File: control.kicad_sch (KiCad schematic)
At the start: 6 parts

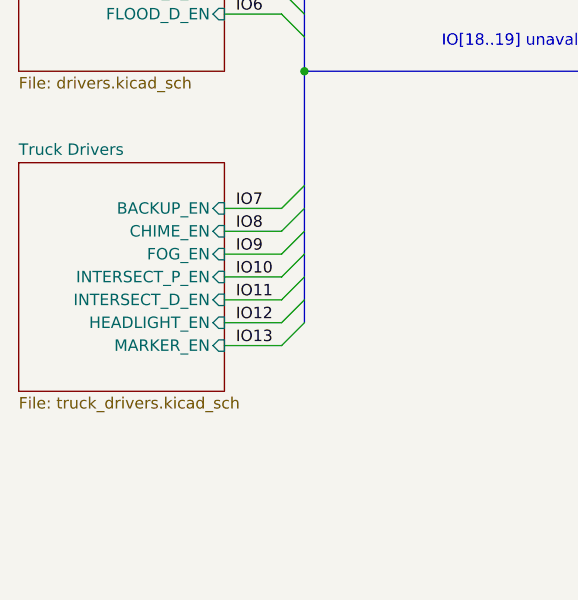
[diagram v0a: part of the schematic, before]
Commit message: add horn circuit
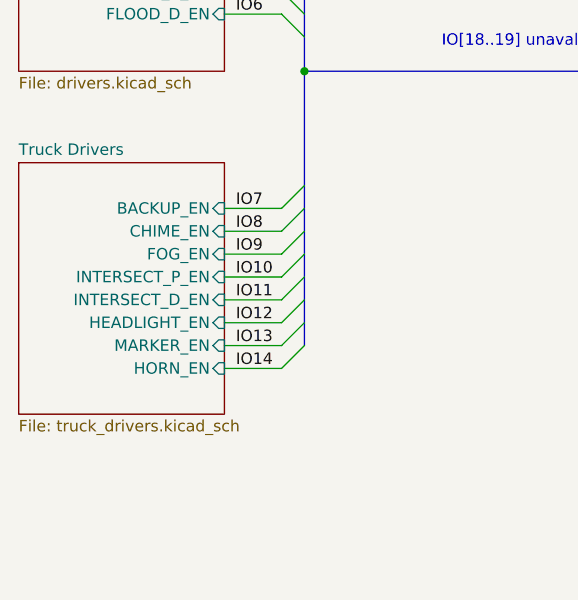
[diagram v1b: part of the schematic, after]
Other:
- sheet Truck Drivers ports: added HORN_EN; removed none
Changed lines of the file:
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@@
+    (stroke (width 0) (type default) (color 0 0 0 0))
+  )
+  (bus_entry (at 86.36 120.65) (size 2.54 -2.54)
     (stroke (width 0) (type default) (color 0 0 0 0))
   )
@@
     (stroke (width 0) (type default) (color 0 0 0 0))
   )
+  (bus (pts (xy 88.9 115.57) (xy 88.9 118.11))
+    (stroke (width 0) (type default) (color 0 0 0 0))
+  )
   (wire (pts (xy 234.95 147.32) (xy 237.49 147.32))
     (stroke (width 0) (type default) (color 0 0 0 0))
@@
   )
   (wire (pts (xy 234.95 144.78) (xy 237.49 144.78))
+    (stroke (width 0) (type default) (color 0 0 0 0))
+  )
+  (wire (pts (xy 80.01 120.65) (xy 86.36 120.65))
     (stroke (width 0) (type default) (color 0 0 0 0))
   )
@@
   )
   (label "IO4" (at 186.69 46.99 0)
+    (effects (font (size 1.27 1.27)) (justify left bottom))
+  )
+  (label "IO14" (at 81.28 120.65 0)
     (effects (font (size 1.27 1.27)) (justify left bottom))
   )
@@
     )
   )
-  (sheet (at 57.15 97.79) (size 22.86 25.4) (fields_autoplaced)
+  (sheet (at 57.15 97.79) (size 22.86 27.94) (fields_autoplaced)
     (stroke (width 0.1524) (type solid) (color 0 0 0 0))
     (fill (color 255 242 138 1.0000))
@@
       (effects (font (size 1.27 1.27)) (justify left bottom))
     )
-    (property "Sheet file" "truck_drivers.kicad_sch" (id 1) (at 57.15 123.7746 0)
+    (property "Sheet file" "truck_drivers.kicad_sch" (id 1) (at 57.15 126.3146 0)
       (effects (font (size 1.27 1.27)) (justify left top))
     )
@@
     )
     (pin "MARKER_EN" input (at 80.01 118.11 0)
+      (effects (font (size 1.27 1.27)) (justify right))
+    )
+    (pin "HORN_EN" input (at 80.01 120.65 0)
       (effects (font (size 1.27 1.27)) (justify right))
     )
@@
       (reference "#PWR?") (unit 1) (value "GNDREF") (footprint "")
     )
+    (path "/9a43fd97-6c7b-45d8-a49e-7ebcbf8082c1/74fb88ab-b729-4031-aa3e-dde0d838ac7e"
+      (reference "#PWR?") (unit 1) (value "+12C") (footprint "")
+    )
     (path "/9a43fd97-6c7b-45d8-a49e-7ebcbf8082c1/7703f52a-ee8a-4214-ad6d-ebef359cb9dc"
       (reference "#PWR?") (unit 1) (value "+12C") (footprint "")
@@
       (reference "#PWR?") (unit 1) (value "GNDREF") (footprint "")
     )
+    (path "/9a43fd97-6c7b-45d8-a49e-7ebcbf8082c1/e296df88-559b-4bed-b46b-c59dd5b7a686"
+      (reference "#PWR?") (unit 1) (value "GNDREF") (footprint "")
+    )
     (path "/9a43fd97-6c7b-45d8-a49e-7ebcbf8082c1/e80195ea-ff8c-45f0-a7ff-9d3c4efd05ec"
       (reference "#PWR?") (unit 1) (value "GNDREF") (footprint "")
@@
       (reference "C?") (unit 1) (value "1uF") (footprint "")
     )
+    (path "/9a43fd97-6c7b-45d8-a49e-7ebcbf8082c1/3e9daf16-d0cb-45c2-9ce8-4b5fda9dce3e"
+      (reference "D?") (unit 1) (value "D") (footprint "")
+    )
     (path "/7dae9e6f-6bdd-4491-8ee1-2da2ec3e3f7f/182708b8-2ceb-4343-8e74-9bff63cfcddf"
       (reference "J?") (unit 1) (value "TE_Faston_20-16AWG_Straight_Tab") (footprint "TE_Faston_20-16AWG_Straight_Tab")
@@
       (reference "J?") (unit 1) (value "TE_Faston_20-16AWG_Straight_Tab") (footprint "TE_Faston_20-16AWG_Straight_Tab")
     )
+    (path "/9a43fd97-6c7b-45d8-a49e-7ebcbf8082c1/c8797b86-23cf-4edf-91b5-8b2b3c3a3d28"
+      (reference "J?") (unit 1) (value "TE_Faston_20-16AWG_Straight_Tab") (footprint "TE_Faston_20-16AWG_Straight_Tab")
+    )
     (path "/9a43fd97-6c7b-45d8-a49e-7ebcbf8082c1/dda25721-7381-499a-b1c9-0386dda14106"
       (reference "J?") (unit 1) (value "TE_Faston_20-16AWG_Straight_Tab") (footprint "TE_Faston_20-16AWG_Straight_Tab")
@@
       (reference "J?") (unit 1) (value "TE_Faston_20-16AWG_Straight_Tab") (footprint "TE_Faston_20-16AWG_Straight_Tab")
     )
+    (path "/9a43fd97-6c7b-45d8-a49e-7ebcbf8082c1/907c764c-051a-490a-a58c-435ca2736f38"
+      (reference "Q?") (unit 1) (value "ZXTN08400BFFCT") (footprint "Package_TO_SOT_SMD:SOT-23")
+    )
     (path "/9a43fd97-6c7b-45d8-a49e-7ebcbf8082c1/032e5309-73a3-4ce6-84c5-57c722d6653d"
       (reference "R?") (unit 1) (value "10k") (footprint "")
@@
     )
     (path "/9a43fd97-6c7b-45d8-a49e-7ebcbf8082c1/2a74df45-1d4c-4c91-8a5f-222daa645f7f"
+      (reference "R?") (unit 1) (value "10k") (footprint "")
+    )
+    (path "/9a43fd97-6c7b-45d8-a49e-7ebcbf8082c1/2cd04b0d-3341-49ad-9223-26d87b31a83d"
       (reference "R?") (unit 1) (value "10k") (footprint "")
     )
@@
       (reference "R?") (unit 1) (value "10k") (footprint "")
     )
+    (path "/9a43fd97-6c7b-45d8-a49e-7ebcbf8082c1/db1e4d6d-d222-4026-a908-ea9cea0b7c0c"
+      (reference "R?") (unit 1) (value "10k") (footprint "")
+    )

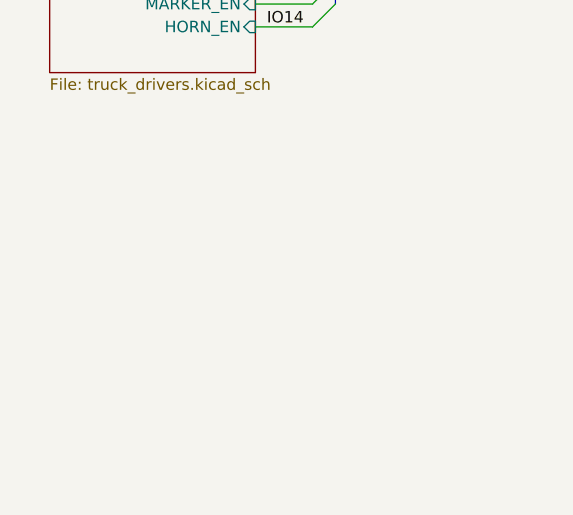
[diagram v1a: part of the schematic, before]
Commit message: add signal inputs
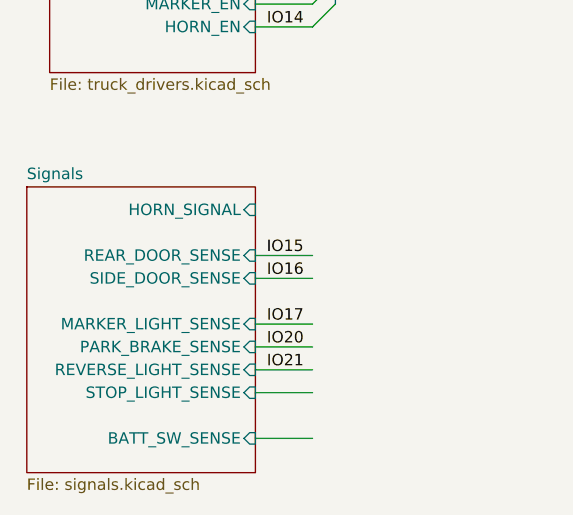
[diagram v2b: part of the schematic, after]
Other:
- added sheet Signals (signals.kicad_sch)

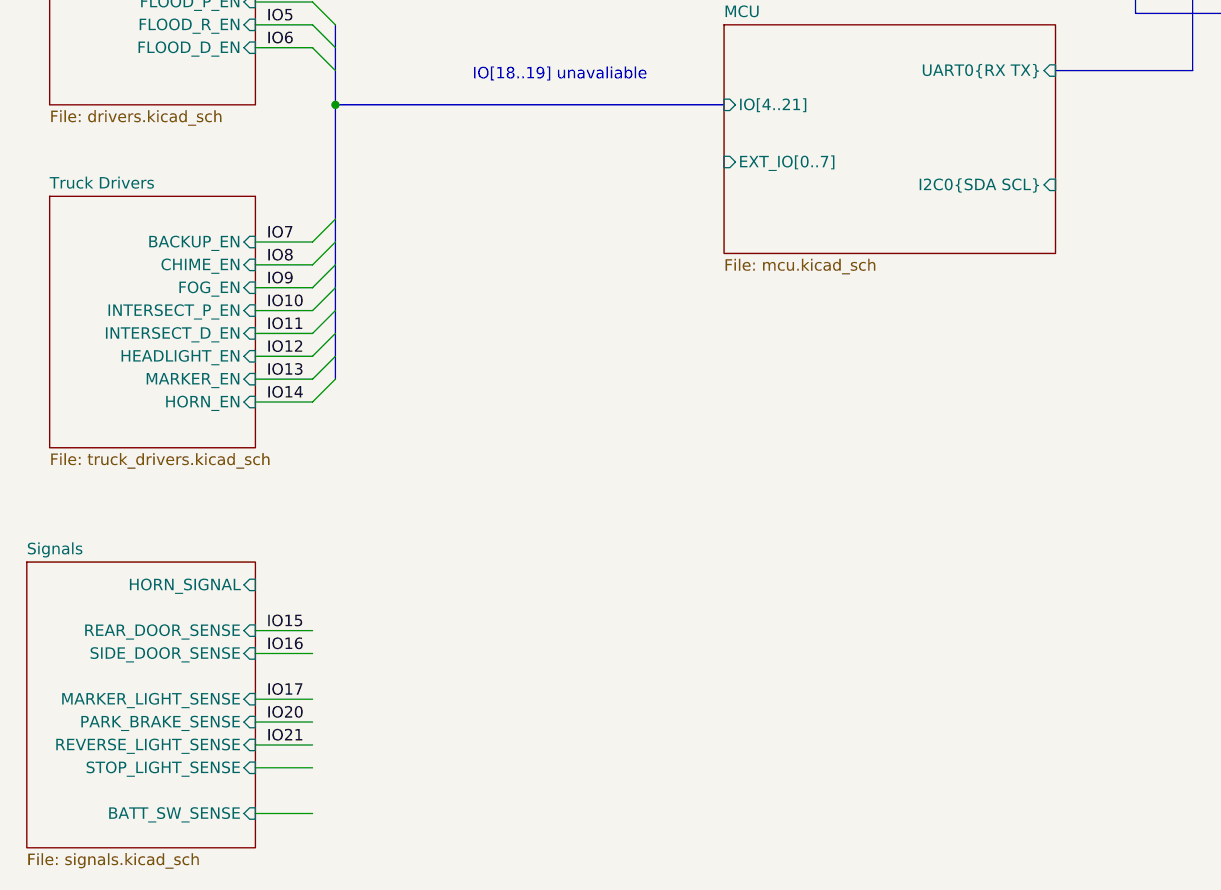
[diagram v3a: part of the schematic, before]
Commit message: add horn jumper to allow mcu or hardware control
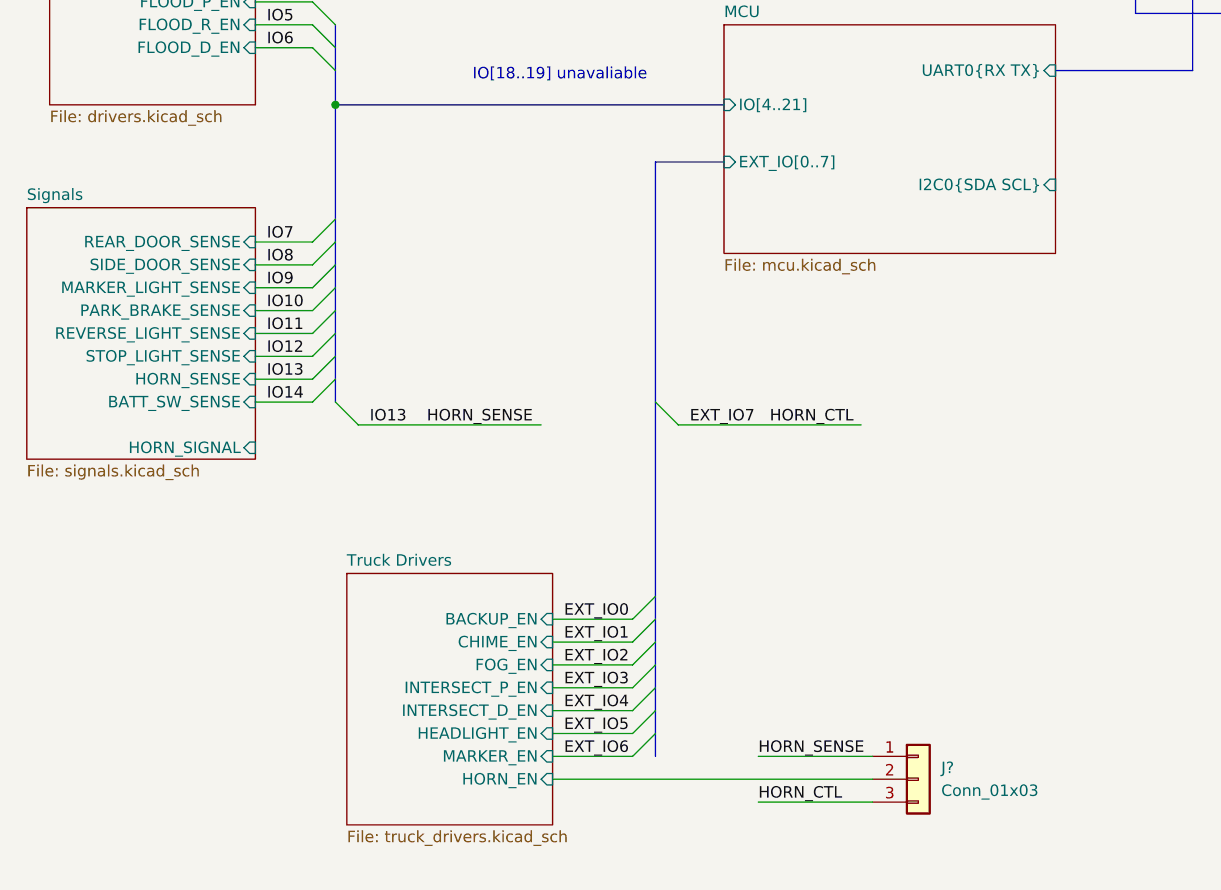
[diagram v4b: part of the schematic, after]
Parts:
- added J?: Conn_01x03, symbol Connector_Generic:Conn_01x03
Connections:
- new net EXT_IO7: J?.3 (Pin_3)
- new net HORN_SENSE: J?.1 (Pin_1)
- new net Truck Drivers/HORN_EN: J?.2 (Pin_2)
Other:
- sheet Signals ports: added HORN_SENSE; removed none

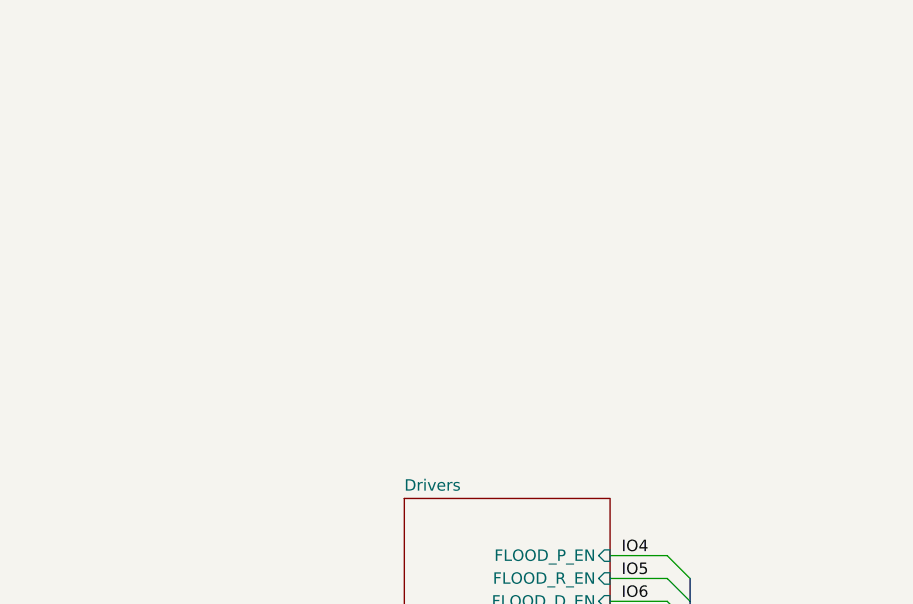
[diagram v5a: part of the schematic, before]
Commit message: add power input
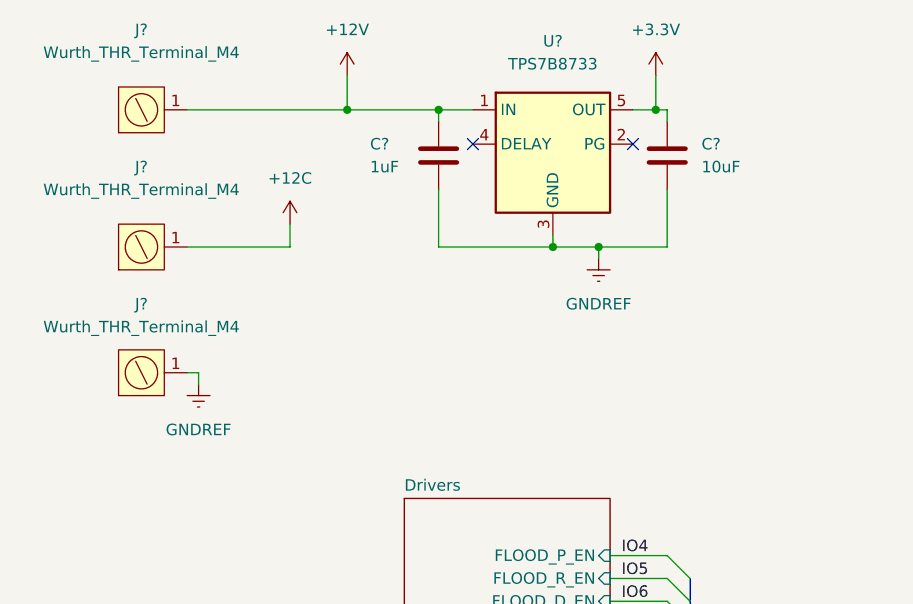
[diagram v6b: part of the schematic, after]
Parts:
- added C?: 10uF, Capacitor_SMD:C_0805_2012Metric_Pad1.18x1.45mm_HandSolder, symbol Device:C
- added C?: 1uF, Capacitor_SMD:C_0805_2012Metric_Pad1.18x1.45mm_HandSolder, symbol Device:C
- added J? (x3): Wurth_THR_Terminal_M4, Toadly:Wurth_THR_Terminal_M4, symbol Toadly:Wurth_THR_Terminal_M4
- added U?: TPS7B8733, Package_TO_SOT_SMD:TO-252-5_TabPin3, symbol Toadly:TPS7B8733
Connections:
- net +12V: now also C?.1, J?.1, U?.1 (IN)
- net +3.3V: now also C?.1, U?.5 (OUT)
- net GNDREF: now also C?.2, C?.2, J?.1, U?.3 (GND)
- new net +12C: J?.1
- no-connect marks 22 -> 24

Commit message: annotate schematic
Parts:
- C3, C4: renamed from C?; footprint (none) -> Capacitor_SMD:C_0805_2012Metric_Pad1.18x1.45mm_HandSolder
- gave numbers to parts that had none: 11

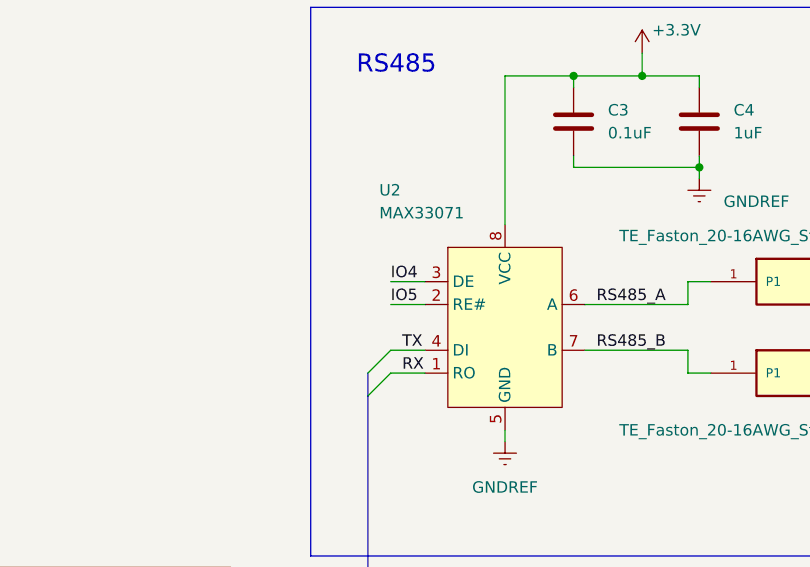
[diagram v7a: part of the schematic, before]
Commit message: fix RS485 control IO
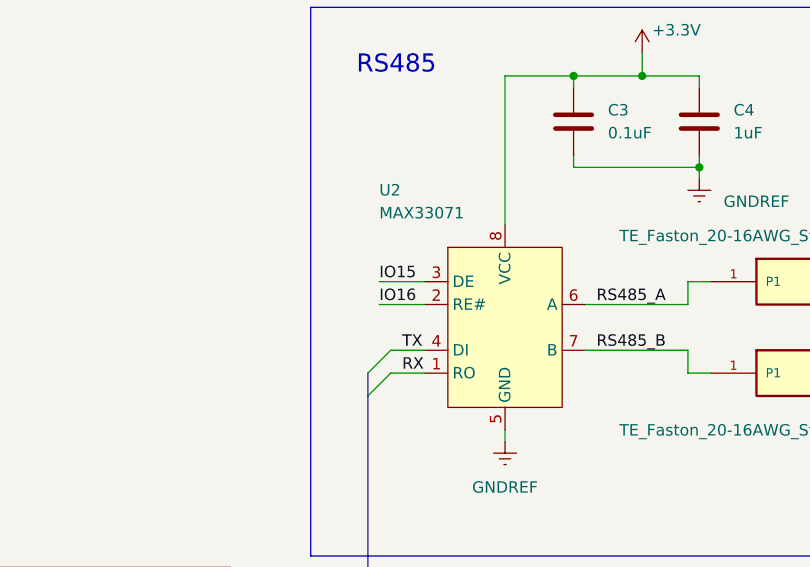
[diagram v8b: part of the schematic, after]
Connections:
- net IO4: no longer U2.3 (DE)
- net IO5: no longer U2.2 (RE#)
- new net IO15: U2.3 (DE)
- new net IO16: U2.2 (RE#)
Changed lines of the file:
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@@
     (stroke (width 0) (type default) (color 0 0 0 0))
   )
-  (wire (pts (xy 186.69 49.53) (xy 190.5 49.53))
+  (wire (pts (xy 185.42 49.53) (xy 190.5 49.53))
     (stroke (width 0) (type default) (color 0 0 0 0))
   )
@@
     (stroke (width 0) (type default) (color 0 0 0 0))
   )
-  (wire (pts (xy 186.69 46.99) (xy 190.5 46.99))
+  (wire (pts (xy 185.42 46.99) (xy 190.5 46.99))
     (stroke (width 0) (type default) (color 0 0 0 0))
   )
@@
     (effects (font (size 1.27 1.27)) (justify left bottom))
   )
-  (label "IO4" (at 186.69 46.99 0)
+  (label "IO15" (at 185.42 46.99 0)
     (effects (font (size 1.27 1.27)) (justify left bottom))
   )
@@
     (effects (font (size 1.27 1.27)) (justify left bottom))
   )
-  (label "IO5" (at 186.69 49.53 0)
-    (effects (font (size 1.27 1.27)) (justify left bottom))
-  )
+  (label "IO16" (at 185.42 49.53 0)
+    (effects (font (size 1.27 1.27)) (justify left bottom))
+  )
